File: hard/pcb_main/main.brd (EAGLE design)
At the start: 230 x 150 mm, 868 parts

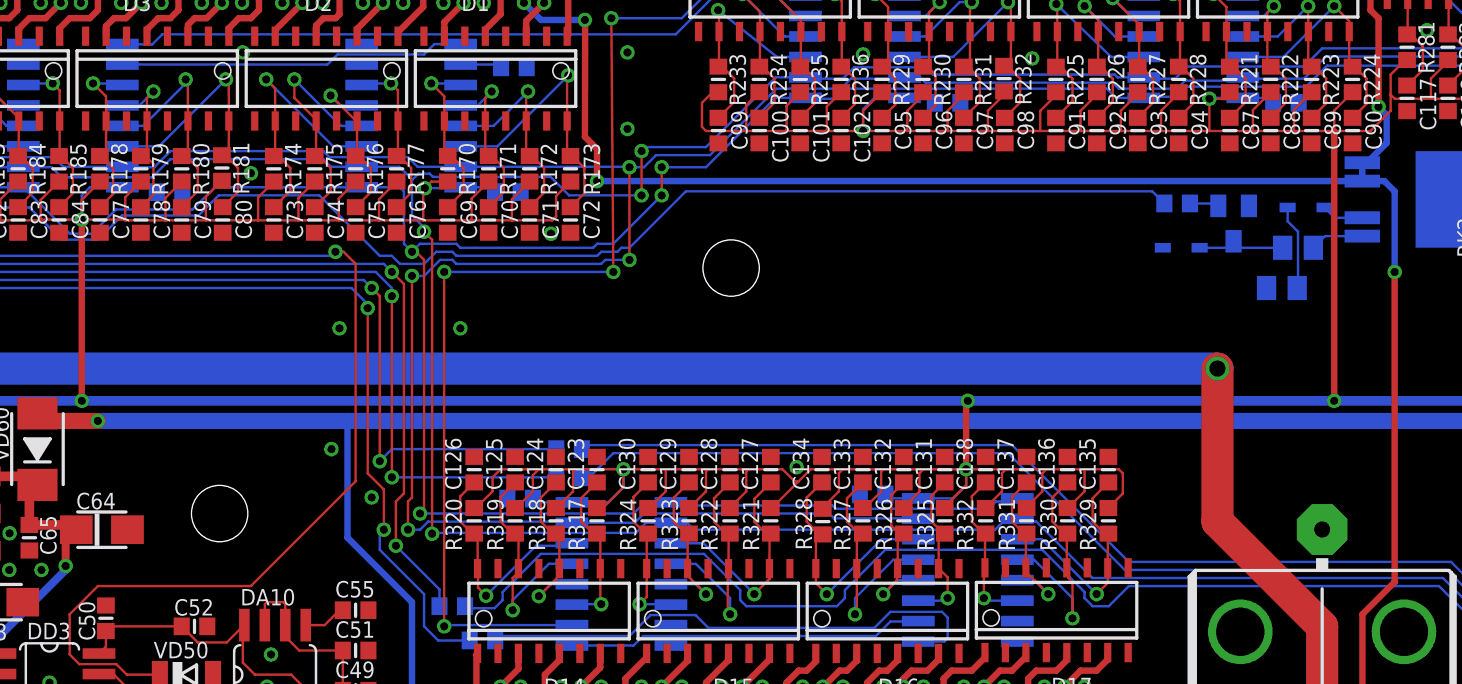
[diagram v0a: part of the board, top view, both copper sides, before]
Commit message: fixed additional mounting holes
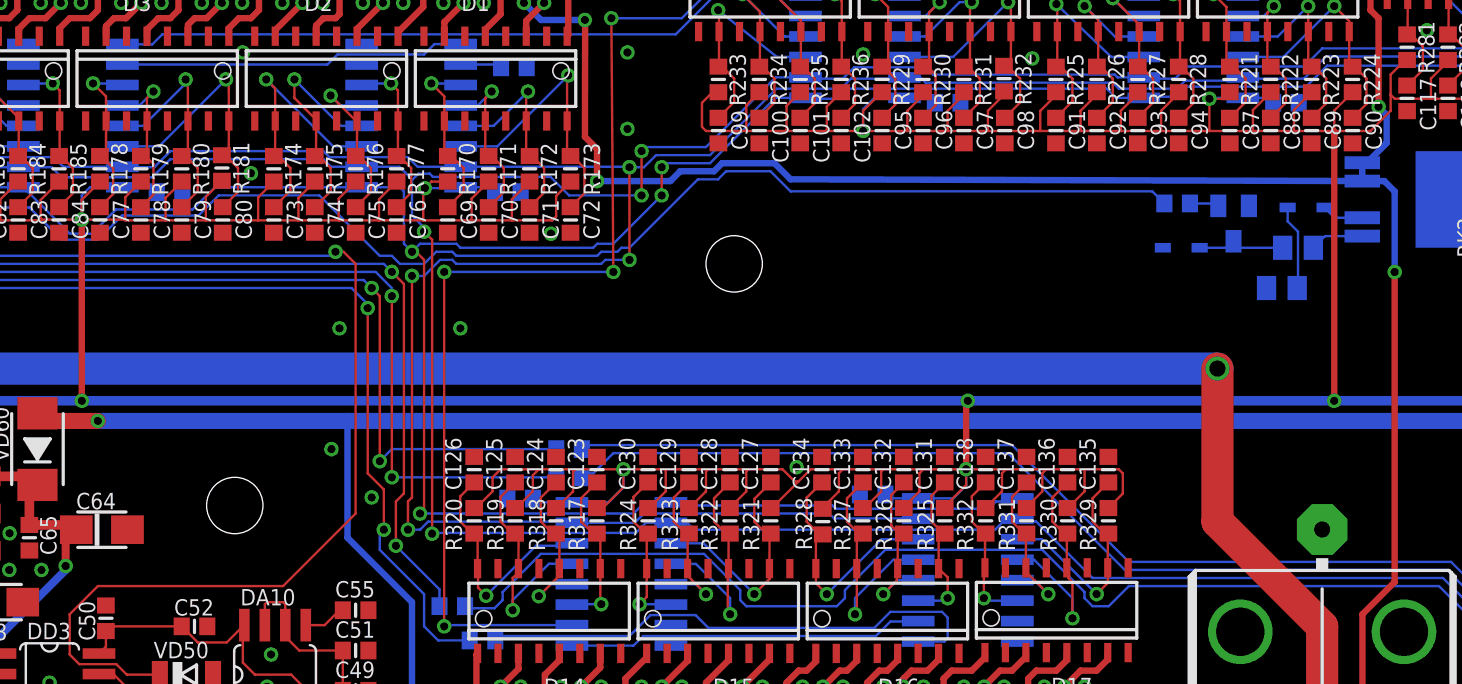
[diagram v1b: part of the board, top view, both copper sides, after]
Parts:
- moved JP10 1.06 mm to (100.0, 64.0)
- moved JP9 0.32 mm to (131.0, 79.0)
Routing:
- net N$349: track 86.3 -> 87.5 mm
- net N$354: track 95.6 -> 96.7 mm
- net Z_CHECK: track 417.5 -> 418.3 mm
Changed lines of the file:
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@@
 <setting verticaltext="up"/>
 </settings>
-<grid distance="0.05" unitdist="inch" unit="inch" style="lines" multiple="1" display="yes" altdistance="0.025" altunitdist="inch" altunit="inch"/>
+<grid distance="1" unitdist="mm" unit="mm" style="lines" multiple="1" display="yes" altdistance="0.1" altunitdist="mm" altunit="mm"/>
 <layers>
 <layer number="1" name="Top" color="4" fill="1" visible="yes" active="yes"/>
@@
 <wire x1="0" y1="150" x2="0" y2="0" width="0" layer="20"/>
 <wire x1="115" y1="156" x2="115" y2="-10.5" width="0.15" layer="48" style="dashdot"/>
-<wire x1="-5" y1="75" x2="243" y2="75" width="0.15" layer="48" style="dashdot"/>
+<wire x1="-14" y1="75" x2="243" y2="75" width="0.15" layer="48" style="dashdot"/>
 <wire x1="-10.5" y1="3.5" x2="242" y2="3.5" width="0.15" layer="48"/>
 <wire x1="-11.5" y1="146.5" x2="239" y2="146.5" width="0.15" layer="48"/>
 <wire x1="20" y1="160" x2="20" y2="-10" width="0.15" layer="48"/>
 <wire x1="210" y1="160" x2="210" y2="-9" width="0.15" layer="48"/>
-<wire x1="3.5" y1="160" x2="3.5" y2="-16" width="0.15" layer="48"/>
-<wire x1="226.5" y1="159" x2="226.5" y2="-16" width="0.15" layer="48"/>
-<dimension x1="115" y1="-9" x2="20" y2="-9" x3="67.5" y3="-9" layer="48"/>
-<dimension x1="115" y1="-9" x2="210" y2="-9" x3="162.5" y3="-9" layer="48"/>
-<dimension x1="3.5" y1="-16" x2="226.5" y2="-16" x3="115" y3="-16" layer="48"/>
-<dimension x1="-10.5" y1="3.5" x2="-10.5" y2="146.5" x3="-10.5" y3="75" layer="48"/>
+<wire x1="3.5" y1="160" x2="3.5" y2="-4" width="0.15" layer="48"/>
+<wire x1="226.5" y1="159" x2="226.5" y2="-4" width="0.15" layer="48"/>
+<dimension x1="115" y1="-9" x2="20" y2="-9" x3="67.5" y3="-14.78" layer="48"/>
+<dimension x1="115" y1="-9" x2="210" y2="-9" x3="162.5" y3="-14.78" layer="48"/>
+<dimension x1="3.5" y1="-4" x2="226.5" y2="-4" x3="115" y3="-23.05" layer="48"/>
+<dimension x1="-10.5" y1="3.5" x2="-10.5" y2="146.5" x3="-20.74" y3="75" layer="48"/>
 <wire x1="108" y1="3.5" x2="122" y2="3.5" width="0.15" layer="42" curve="-180"/>
 <wire x1="108" y1="3.5" x2="108" y2="0" width="0.15" layer="42" style="dashdot"/>
@@
 <wire x1="67.5" y1="95" x2="67.5" y2="53" width="1.2" layer="30"/>
 <wire x1="67.5" y1="53" x2="15" y2="53" width="1.2" layer="30"/>
+<dimension x1="131" y1="79" x2="115" y2="-8" x3="123" y3="-8" layer="48" dtype="horizontal"/>
+<dimension x1="99" y1="64" x2="-14" y2="75" x3="-12" y3="69.5" layer="48" dtype="vertical"/>
+<dimension x1="131" y1="79" x2="-13" y2="75" x3="-7" y3="77" layer="48" dtype="vertical"/>
+<wire x1="95" y1="64" x2="104" y2="64" width="0.15" layer="48"/>
+<wire x1="131" y1="85" x2="131" y2="79" width="0.15" layer="48"/>
+<wire x1="131" y1="79" x2="131" y2="78" width="0.15" layer="48"/>
+<wire x1="131" y1="79" x2="138" y2="79" width="0.15" layer="48"/>
+<dimension x1="100" y1="63" x2="115" y2="-8" x3="107.5" y3="-8" layer="48" dtype="horizontal"/>
+<wire x1="100" y1="63" x2="100" y2="68" width="0.15" layer="48"/>
 </plain>
 <attributes>
@@
 <attribute name="VALUE" x="65.5675" y="68.3725" size="0.8128" layer="27"/>
 </element>
-<element name="JP9" library="mount" package="STAND-OFF" value="STAND-OFF-M4" x="130.81" y="78.74">
-<attribute name="DATABASE" value="./bom/volat3-PARTSDB.tsv" x="130.81" y="78.74" size="1.778" layer="27" display="off"/>
+<element name="JP9" library="mount" package="STAND-OFF" value="STAND-OFF-M4" x="131" y="79">
+<attribute name="DATABASE" value="./bom/volat3-PARTSDB.tsv" x="131" y="79" size="1.778" layer="27" display="off"/>
 </element>
-<element name="JP10" library="mount" package="STAND-OFF" value="STAND-OFF-M4" x="99.06" y="63.5">
-<attribute name="DATABASE" value="./bom/volat3-PARTSDB.tsv" x="99.06" y="63.5" size="1.778" layer="27" display="off"/>
+<element name="JP10" library="mount" package="STAND-OFF" value="STAND-OFF-M4" x="100" y="64">
+<attribute name="DATABASE" value="./bom/volat3-PARTSDB.tsv" x="100" y="64" size="1.778" layer="27" display="off"/>
 </element>
 </elements>
@@
 <wire x1="173.0275" y1="104.0275" x2="170.5" y2="101.5" width="0.4" layer="16"/>
 <wire x1="170.5" y1="101.5" x2="168.75" y2="99.875" width="0.4" layer="16"/>
-<wire x1="169.99" y1="84.14" x2="122.485" y2="84.14" width="0.4" layer="16"/>
+<wire x1="169.99" y1="84.14" x2="134.5" y2="84.25" width="0.4" layer="16"/>
+<wire x1="134.5" y1="84.25" x2="133.5" y2="85.25" width="0.4" layer="16"/>
+<wire x1="133.5" y1="85.25" x2="130.25" y2="85.25" width="0.4" layer="16"/>
 <wire x1="169.99" y1="84.14" x2="171.36" y2="84.14" width="0.4" layer="16"/>
 <wire x1="171.36" y1="84.14" x2="172" y2="83.5" width="0.4" layer="16"/>
@@
 <wire x1="121.75" y1="94.125" x2="121.735" y2="94.14" width="0.15" layer="1"/>
 <wire x1="170" y1="57.25" x2="170" y2="51" width="0.4" layer="1"/>
+<wire x1="130.25" y1="85.25" x2="129.75" y2="84.75" width="0.4" layer="16"/>
+<wire x1="129.75" y1="84.75" x2="127.65" y2="84.75" width="0.4" layer="16"/>
+<wire x1="127.65" y1="84.75" x2="127.04" y2="84.14" width="0.4" layer="16"/>
+<wire x1="127.04" y1="84.14" x2="122.485" y2="84.14" width="0.4" layer="16"/>
 </signal>
 <signal name="DISCRETE_33">
@@
 <wire x1="111.75" y1="63.75" x2="111.5" y2="63.5" width="0.15" layer="1"/>
 <via x="111.5" y="63.5" extent="1-16" drill="0.5"/>
-<wire x1="133.555" y1="89.305" x2="129.25" y2="85" width="0.15" layer="16"/>
-<wire x1="129.25" y1="85" x2="126.5" y2="85" width="0.15" layer="16"/>
+<wire x1="133.555" y1="89.305" x2="129.5" y2="85.25" width="0.15" layer="16"/>
+<wire x1="129.5" y1="85.25" x2="126.75" y2="85.25" width="0.15" layer="16"/>
+<wire x1="126.75" y1="85.25" x2="126.5" y2="85" width="0.15" layer="16"/>
 <via x="126.5" y="85" extent="1-16" drill="0.5"/>
 <wire x1="126.5" y1="85" x2="126.5" y2="83.25" width="0.15" layer="1"/>
@@
 <wire x1="89.75" y1="54.75" x2="89.75" y2="57.25" width="0.15" layer="1"/>
 <wire x1="89.75" y1="57.25" x2="91.5" y2="59" width="0.15" layer="1"/>
-<wire x1="91.5" y1="59" x2="101" y2="59" width="0.15" layer="1"/>
-<wire x1="101" y1="59" x2="107.5" y2="65.5" width="0.15" layer="1"/>
-<wire x1="107.5" y1="65.5" x2="107.5" y2="79" width="0.15" layer="1"/>
+<wire x1="91.5" y1="59" x2="103" y2="59" width="0.15" layer="1"/>
+<wire x1="103" y1="59" x2="107.5" y2="63.5" width="0.15" layer="1"/>
+<wire x1="107.5" y1="63.5" x2="107.5" y2="79" width="0.15" layer="1"/>
 <via x="106.25" y="79.75" extent="1-16" drill="0.5"/>
 <wire x1="107.5" y1="79" x2="106.75" y2="79.75" width="0.15" layer="1"/>
@@
 <contactref element="R24" pad="2"/>
 <wire x1="157.7062" y1="82.75" x2="156.9562" y2="83.5" width="0.15" layer="16"/>
-<wire x1="156.9562" y1="83.5" x2="128" y2="83.5" width="0.15" layer="16"/>
-<wire x1="128" y1="83.5" x2="124.5" y2="80" width="0.15" layer="16"/>
+<wire x1="156.9562" y1="83.5" x2="134.5" y2="83.5" width="0.15" layer="16"/>
+<wire x1="134.5" y1="83.5" x2="133.25" y2="84.75" width="0.15" layer="16"/>
+<wire x1="133.25" y1="84.75" x2="130.5" y2="84.75" width="0.15" layer="16"/>
+<wire x1="130.5" y1="84.75" x2="130" y2="84.25" width="0.15" layer="16"/>
+<wire x1="130" y1="84.25" x2="128.75" y2="84.25" width="0.15" layer="16"/>
+<wire x1="128.75" y1="84.25" x2="124.5" y2="80" width="0.15" layer="16"/>
 <wire x1="109" y1="79.5" x2="105.25" y2="83.25" width="0.15" layer="16"/>
 <wire x1="105.25" y1="83.25" x2="99" y2="83.25" width="0.15" layer="16"/>

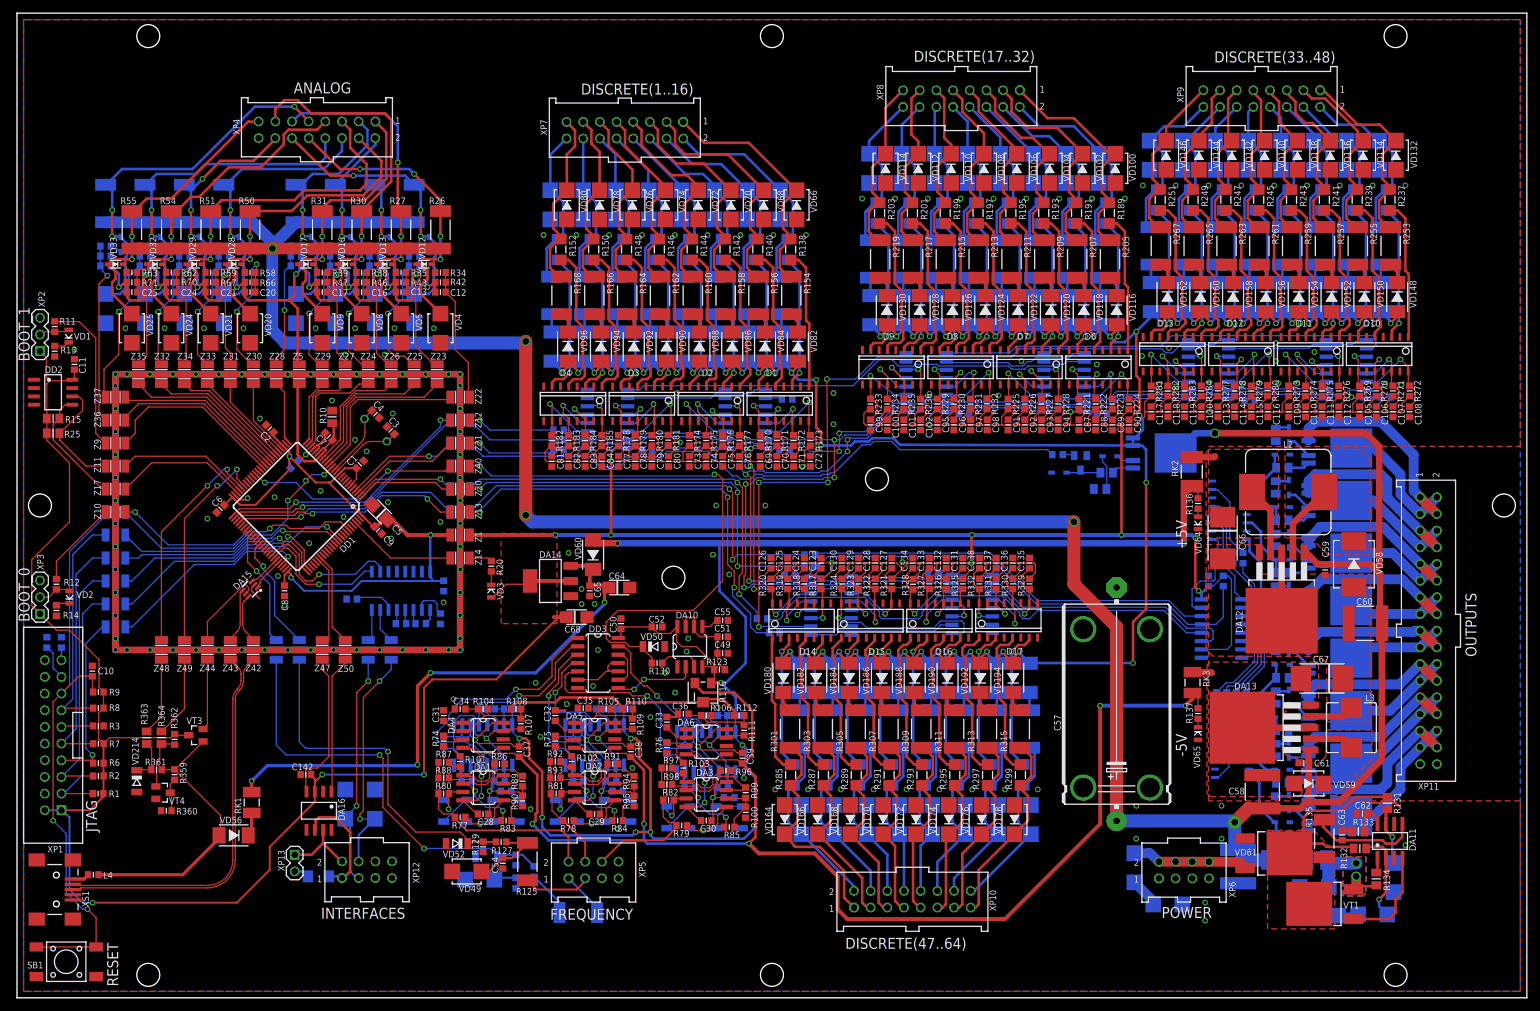
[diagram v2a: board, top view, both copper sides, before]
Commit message: fixed mount holes diameter
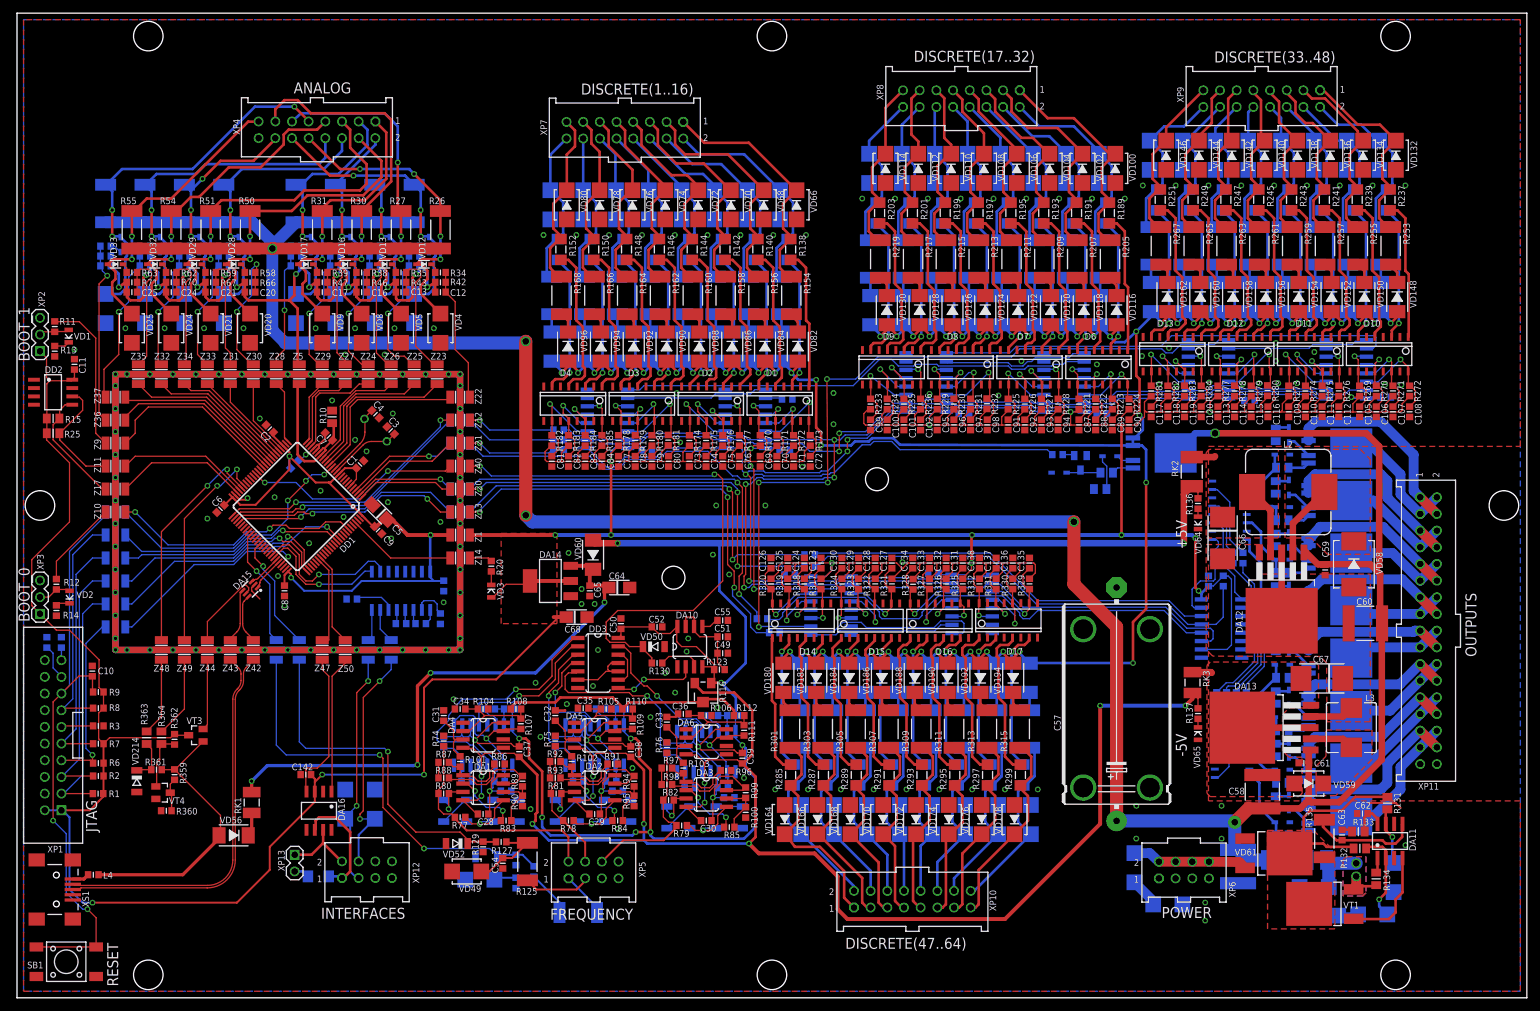
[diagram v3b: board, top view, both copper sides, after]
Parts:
- JP1, JP2, JP3, JP4, JP5, JP6, JP7, JP8: device mount:STAND-OFF -> mount:STAND-OFF-M4
- JP10, JP9: value STAND-OFF-M4 -> STAND-OFF-M3; device mount:STAND-OFF -> mount:STAND-OFF-M3
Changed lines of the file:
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@@
 <layer number="106" name="bPlate" color="7" fill="1" visible="no" active="yes"/>
 <layer number="107" name="Crop" color="7" fill="1" visible="no" active="yes"/>
+<layer number="116" name="Patch_BOT" color="9" fill="4" visible="yes" active="yes"/>
 <layer number="121" name="_tsilk" color="7" fill="1" visible="no" active="yes"/>
 <layer number="122" name="_bsilk" color="7" fill="1" visible="no" active="yes"/>
@@
 <layer number="220" name="220bmp" color="21" fill="1" visible="no" active="no"/>
 <layer number="221" name="221bmp" color="22" fill="1" visible="no" active="no"/>
+<layer number="222" name="222bmp" color="23" fill="1" visible="no" active="no"/>
 <layer number="223" name="223bmp" color="24" fill="1" visible="no" active="no"/>
 <layer number="224" name="224bmp" color="25" fill="1" visible="no" active="no"/>
@@
 <attribute name="PARTNO" value="IN74HC595AD" x="183.5" y="56.25" size="1.778" layer="28" rot="MR270" display="off"/>
 </element>
-<element name="JP8" library="mount" package="STAND-OFF" value="STAND-OFF-M4" x="20" y="3.5" locked="yes">
+<element name="JP8" library="mount" package="STAND-OFF-M4" value="STAND-OFF-M4" x="20" y="3.5" locked="yes">
 <attribute name="BOM" value="EXCLUDE" x="20" y="3.5" size="1.778" layer="27" display="off"/>
 </element>
-<element name="JP7" library="mount" package="STAND-OFF" value="STAND-OFF-M4" x="115" y="3.5" locked="yes">
+<element name="JP7" library="mount" package="STAND-OFF-M4" value="STAND-OFF-M4" x="115" y="3.5" locked="yes">
 <attribute name="BOM" value="EXCLUDE" x="115" y="3.5" size="1.778" layer="27" display="off"/>
 </element>
-<element name="JP6" library="mount" package="STAND-OFF" value="STAND-OFF-M4" x="210" y="3.5" locked="yes">
+<element name="JP6" library="mount" package="STAND-OFF-M4" value="STAND-OFF-M4" x="210" y="3.5" locked="yes">
 <attribute name="BOM" value="EXCLUDE" x="210" y="3.5" size="1.778" layer="27" display="off"/>
 </element>
-<element name="JP5" library="mount" package="STAND-OFF" value="STAND-OFF-M4" x="3.5" y="75" locked="yes">
+<element name="JP5" library="mount" package="STAND-OFF-M4" value="STAND-OFF-M4" x="3.5" y="75" locked="yes">
 <attribute name="BOM" value="EXCLUDE" x="3.5" y="75" size="1.778" layer="27" display="off"/>
 </element>
-<element name="JP4" library="mount" package="STAND-OFF" value="STAND-OFF-M4" x="226.5" y="75" locked="yes">
+<element name="JP4" library="mount" package="STAND-OFF-M4" value="STAND-OFF-M4" x="226.5" y="75" locked="yes">
 <attribute name="BOM" value="EXCLUDE" x="226.5" y="75" size="1.778" layer="27" display="off"/>
 </element>
-<element name="JP3" library="mount" package="STAND-OFF" value="STAND-OFF-M4" x="115" y="146.5" locked="yes">
+<element name="JP3" library="mount" package="STAND-OFF-M4" value="STAND-OFF-M4" x="115" y="146.5" locked="yes">
 <attribute name="BOM" value="EXCLUDE" x="115" y="146.5" size="1.778" layer="27" display="off"/>
 </element>
-<element name="JP2" library="mount" package="STAND-OFF" value="STAND-OFF-M4" x="210" y="146.5" locked="yes">
+<element name="JP2" library="mount" package="STAND-OFF-M4" value="STAND-OFF-M4" x="210" y="146.5" locked="yes">
 <attribute name="BOM" value="EXCLUDE" x="210" y="146.5" size="1.778" layer="27" display="off"/>
 </element>
-<element name="JP1" library="mount" package="STAND-OFF" value="STAND-OFF-M4" x="20" y="146.5" locked="yes">
+<element name="JP1" library="mount" package="STAND-OFF-M4" value="STAND-OFF-M4" x="20" y="146.5" locked="yes">
 <attribute name="BOM" value="EXCLUDE" x="20" y="146.5" size="1.778" layer="27" display="off"/>
 </element>
@@
 <attribute name="PARTNO" value="NFE31PT152Z1E9" x="67.5" y="70.5" size="1.778" layer="27" display="off"/>
 </element>
-<element name="JP9" library="mount" package="STAND-OFF" value="STAND-OFF-M4" x="131" y="79">
-<attribute name="DATABASE" value="./bom/volat3-PARTSDB.tsv" x="131" y="79" size="1.778" layer="27" display="off"/>
-<attribute name="BOM" value="EXCLUDE" x="131" y="79" size="1.778" layer="27" display="off"/>
-</element>
-<element name="JP10" library="mount" package="STAND-OFF" value="STAND-OFF-M4" x="100" y="64">
-<attribute name="DATABASE" value="./bom/volat3-PARTSDB.tsv" x="100" y="64" size="1.778" layer="27" display="off"/>
-<attribute name="BOM" value="EXCLUDE" x="100" y="64" size="1.778" layer="27" display="off"/>
-</element>
+<element name="JP9" library="mount" package="STAND-OFF-M3" value="STAND-OFF-M3" x="131" y="79"/>
+<element name="JP10" library="mount" package="STAND-OFF-M3" value="STAND-OFF-M3" x="100" y="64"/>
 </elements>
 <signals>
